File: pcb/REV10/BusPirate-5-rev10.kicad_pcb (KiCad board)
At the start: 4 copper layers, 80 x 80.2 mm, 217 parts, among them J201 Conn_01x03, J202 TYPE-C-31-M-12, J301 Conn_01x10, J302 Conn_01x09, Q202 2N7002, Q300 SI2301, Q301 SI2301, Q302 SI2301, Q303 SI2301, Q304 SI2301, Q305 SI2301, Q306 SI2301, Q307 SI2301, Q401 BCM857, Q402 SI2301, Q601 MMDT3906, Q602 SI2301, SW101 SW_SPST, SW102 4P_button_sw, U102 W25Q128JVSIQ, U103 RP2040, U105 MT29F1G01ABAFDWB, U301 SN74LVC1T45DCK, U302 SN74LVC1T45DCK, U303 SN74LVC1T45DCK, U304 SN74LVC1T45DCK, U305 SN74LVC1T45DCK, U306 SN74LVC1T45DCK, U307 SN74LVC1T45DCK, U308 SN74LVC1T45DCK, U401 ME6211A33PG-N, U402 CD4067, U403 AP2127, U404 LMV321, U501 74HC595, U502 74HC595, U503 74HCT245PW, U504 LMV324, U505 LMV324, U506 LMV321, U601 LMV321A, U602 LMV331, U603 LMV321, Y101 12Mhz

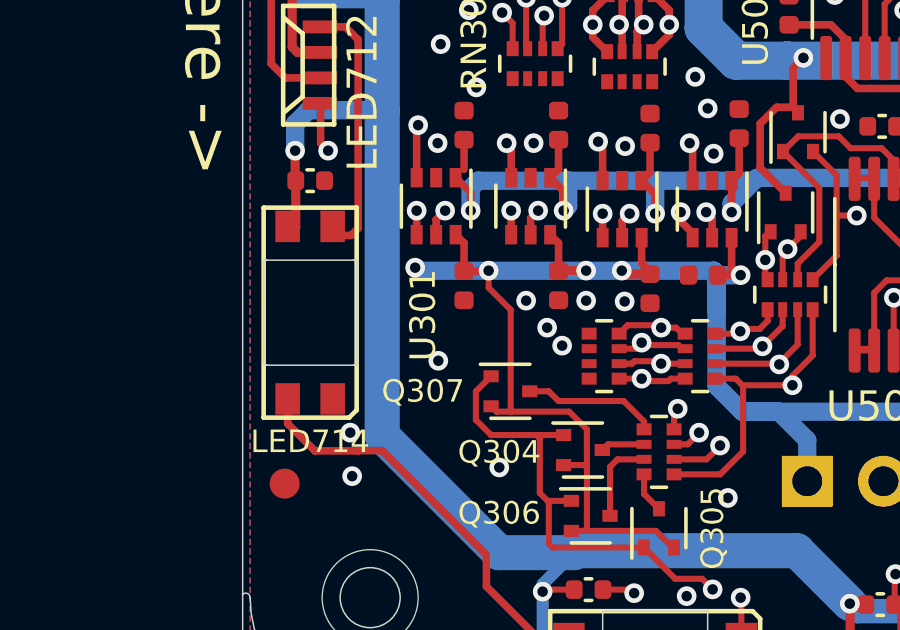
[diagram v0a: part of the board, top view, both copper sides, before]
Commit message: Add pulldown on VREF. Change VUSB MUX series resistor to 510R. May be other value updates that didn't get checked in previously.
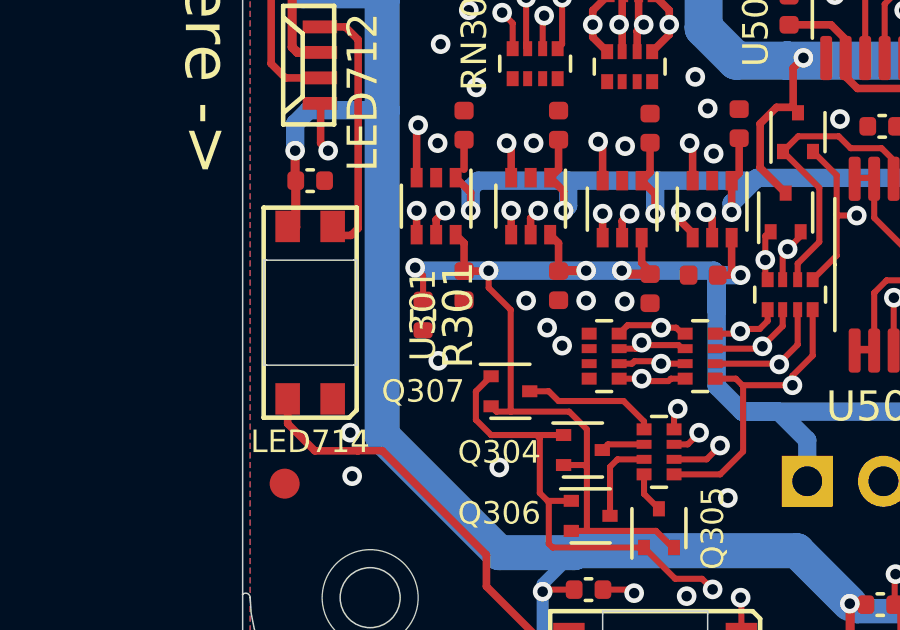
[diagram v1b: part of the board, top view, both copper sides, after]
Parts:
- added R301: 10K, Resistor_SMD:R_0402_1005Metric, F.Cu at (105.7, 106.7)
- R320: value 10K -> 510R
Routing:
- net BUFIO7: track 30.3 -> 29.1 mm
- net VREF_VOUT: track 156.2 -> 157.4 mm
- net BUFIO6: track 26.5 -> 25.5 mm
- net BUFIO5: track 28.2 -> 27.5 mm
- net BUFDIR0: track 37.1 -> 36.5 mm

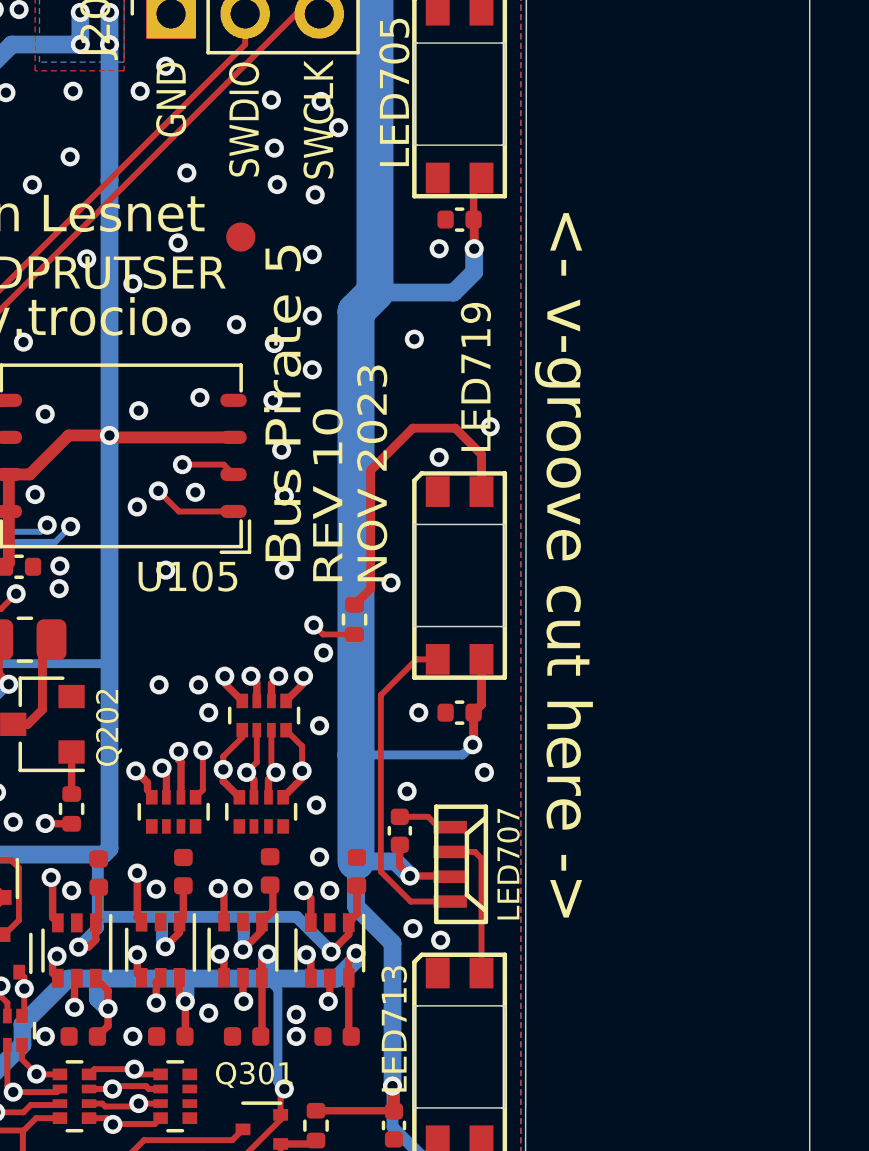
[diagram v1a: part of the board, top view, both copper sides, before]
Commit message: REV10: add missing LED, fix LED placement.
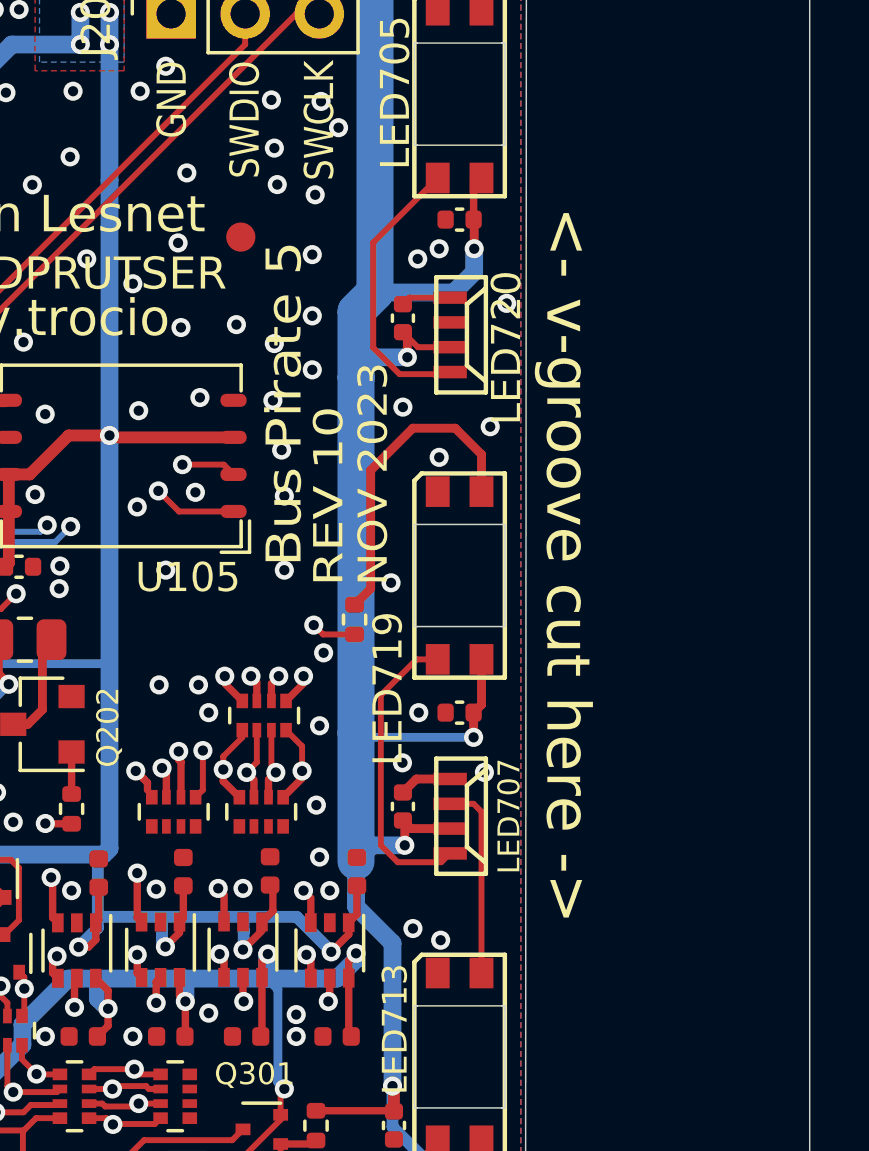
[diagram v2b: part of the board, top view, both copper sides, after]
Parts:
- added C720: 0.1uF, Capacitor_SMD:C_0402_1005Metric, F.Cu at (156.0, 81.3)
- added LED720: SK6812-side-a_b, dp-LED:SK6812-side-a_b, F.Cu at (157.9, 81.8)
- moved LED707 1.65 mm to (157.9, 98.3)
- moved C707 0.84 mm to (156.0, 98.0)
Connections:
- LED705 pad 2: unconnected-(LED705-DO-Pad2) -> Net-(LED705-DO)
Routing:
- net Net-(LED705-DO): track 0.00 -> 9.78 mm
- net +VUSB: track 414.3 -> 419.1 mm, vias 48 -> 49
- net GND: track 53.9 -> 55.6 mm, vias 265 -> 267
- net Net-(LED707-DO): track 5.09 -> 6.72 mm
- net Net-(LED707-DI): track 11.3 -> 10.3 mm

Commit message: rev10 pcb
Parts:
- D500, D501, D502, D503, D504: value BAT54C -> BAS40-05T
- U301, U302, U303, U304, U305, U306, U307, U308: value SN74LVC1T45DCK -> 74LVC1T45
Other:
- board size 80 x 80.2 mm -> 60.5 x 60 mm
- board text removed: "Ian Lesnet"
- board text removed: "SMDPRUTSER"
- board text removed: "v.trocio"
